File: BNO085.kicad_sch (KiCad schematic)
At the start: 0 parts

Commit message: Update schematic and libraries
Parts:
- added U5: BNO085, uSlime-libs:LGA28_5.2X3.8_CEV, symbol uSlime:BNO085
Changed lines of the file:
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@@
 	(generator_version "8.0")
 	(paper "A4")
+	(symbol
+		(lib_id "uSlime:BNO085")
+		(at 74.93 62.23 0)
+		(unit 1)
+		(exclude_from_sim no)
+		(in_bom yes)
+		(on_board yes)
+		(dnp no)
+		(fields_autoplaced yes)
+		(property "Reference" "U5"
+			(at 111.125 52.07 0)
+			(effects
+				(font
+					(size 1.524 1.524)
+				)
+			)
+		)
+		(property "Value" "BNO085"
+			(at 111.125 54.61 0)
+			(effects
+				(font
+					(size 1.524 1.524)
+				)
+			)
+		)
+		(property "Footprint" "uSlime-libs:LGA28_5.2X3.8_CEV"
+			(at 88.9 62.23 0)
+			(effects
+				(font
+					(size 1.27 1.27)
+					(italic yes)
+				)
+				(hide yes)
+			)
+		)
+		(property "Datasheet" "BNO085"
+			(at 88.9 62.23 0)
+			(effects
+				(font
+					(size 1.27 1.27)
+					(italic yes)
+				)
+				(hide yes)
+			)
+		)
+		(property "Description" ""
+			(at 88.9 62.23 0)
+			(effects
+				(font
+					(size 1.27 1.27)
+				)
+				(hide yes)
+			)
+		)
+		(pin "27"
+		)
+		(pin "24"
+		)
+		(pin "4"
+		)
+		(pin "23"
+		)
+		(pin "7"
+		)
+		(pin "28"
+		)
+		(pin "21"
+		)
+		(pin "1"
+		)
+		(pin "6"
+		)
+		(pin "10"
+		)
+		(pin "16"
+		)
+		(pin "18"
+		)
+		(pin "20"
+		)
+		(pin "11"
+		)
+		(pin "25"
+		)
+		(pin "8"
+		)
+		(pin "26"
+		)
+		(pin "13"
+		)
+		(pin "12"
+		)
+		(pin "14"
+		)
+		(pin "2"
+		)
+		(pin "3"
+		)
+		(pin "22"
+		)
+		(pin "19"
+		)
+		(pin "9"
+		)
+		(pin "15"
+		)
+		(pin "5"
+		)
+		(pin "17"
+		)
+		(instances
+			(project "uSlime"
+				(path "/f32c1c49-f803-4e7c-a530-6db148a7ba36/1072de81-ddaf-4115-9b1e-8b480e2a0117"
+					(reference "U5")
+					(unit 1)
+				)
+			)
+		)
+	)
 )

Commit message: Modify ESP32
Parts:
- added C6: 0.1 uF, Capacitor_SMD:C_0603_1608Metric, symbol uSlime:C
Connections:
- net GND: now reaches U5.10 (CLKSEL0)
- net GND: now also U5.2 (GND), U5.25 (GND)
- net +3.3V: now reaches U5.3 (VDD)
- net at U5.9 (CAP): now also C6.2

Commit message: 1st attempt finish BNO085
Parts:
- added C7, C8: 22pF, Capacitor_SMD:C_0603_1608Metric, symbol uSlime:C
- added C9: 0.1 uF, Capacitor_SMD:C_0603_1608Metric, symbol uSlime:C
- added Y1: 32.768, uSlime-libs:OSC-SMD_L3.2-W1.5, symbol uSlime:Crystal
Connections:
- net +3.3V: now also U5.28 (VDDIO), C9.1
- net GND: now also C7.1, C8.1, C9.2
- net BNO_RST: now reaches U5.11 (NRST)
- net BNO_MOSI: now reaches U5.17 (SA0/H_MOSI)
- net BNO_CS: now reaches U5.18 (H_CSN)
- net BNO_SCL: now reaches U5.19 (H_SCL/SCK/RX)
- net BNO_SDA: now reaches U5.20 (H_SDA/H_MISO/TX)
- net at U5.26 (XOUT32/CLKSEL1): now also C7.2, Y1.2
- net at U5.27 (XIN32): now also C8.2, Y1.1

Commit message: update power
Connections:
- net GND: now also C6.1
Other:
- moved on the sheet: Y1
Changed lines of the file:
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@@
 	(paper "A4")
+	(junction
+		(at 157.48 76.2)
+		(diameter 0)
+		(color 0 0 0 0)
+	)
 	(junction
 		(at 68.58 59.69)
@@
 	)
 	(junction
-		(at 157.48 77.47)
-		(diameter 0)
-		(color 0 0 0 0)
-	)
-	(junction
-		(at 165.1 77.47)
-		(diameter 0)
-		(color 0 0 0 0)
-	)
-	(junction
 		(at 83.82 64.77)
 		(diameter 0)
 		(color 0 0 0 0)
 	)
-	(wire
-		(pts
-			(xy 157.48 64.77) (xy 157.48 77.47)
+	(junction
+		(at 165.1 76.2)
+		(diameter 0)
+		(color 0 0 0 0)
+	)
+	(wire
+		(pts
+			(xy 157.48 76.2) (xy 157.48 80.01)
+		)
+		(stroke
+			(width 0)
+			(type default)
+		)
+	)
+	(wire
+		(pts
+			(xy 157.48 64.77) (xy 157.48 76.2)
 		)
 		(stroke
@@
 	(wire
 		(pts
-			(xy 165.1 77.47) (xy 165.1 80.01)
-		)
-		(stroke
-			(width 0)
-			(type default)
-		)
-	)
-	(wire
-		(pts
 			(xy 157.48 90.17) (xy 157.48 87.63)
 		)
@@
 	(wire
 		(pts
+			(xy 165.1 76.2) (xy 165.1 80.01)
+		)
+		(stroke
+			(width 0)
+			(type default)
+		)
+	)
+	(wire
+		(pts
 			(xy 80.01 64.77) (xy 83.82 64.77)
 		)
@@
 	(wire
 		(pts
+			(xy 74.93 82.55) (xy 64.77 82.55)
+		)
+		(stroke
+			(width 0)
+			(type default)
+		)
+	)
+	(wire
+		(pts
 			(xy 134.62 85.09) (xy 133.35 85.09)
 		)
@@
 	(wire
 		(pts
-			(xy 157.48 77.47) (xy 157.48 80.01)
-		)
-		(stroke
-			(width 0)
-			(type default)
-		)
-	)
-	(wire
-		(pts
 			(xy 85.09 85.09) (xy 88.9 85.09)
 		)
@@
 	(wire
 		(pts
+			(xy 64.77 82.55) (xy 64.77 87.63)
+		)
+		(stroke
+			(width 0)
+			(type default)
+		)
+	)
+	(wire
+		(pts
 			(xy 68.58 55.88) (xy 68.58 59.69)
 		)
@@
 	(wire
 		(pts
+			(xy 139.7 62.23) (xy 133.35 62.23)
+		)
+		(stroke
+			(width 0)
+			(type default)
+		)
+	)
+	(wire
+		(pts
 			(xy 134.62 87.63) (xy 133.35 87.63)
 		)
@@
 	(wire
 		(pts
+			(xy 139.7 58.42) (xy 139.7 62.23)
+		)
+		(stroke
+			(width 0)
+			(type default)
+		)
+	)
+	(wire
+		(pts
 			(xy 133.35 64.77) (xy 157.48 64.77)
 		)
@@
 	(wire
 		(pts
-			(xy 140.97 62.23) (xy 133.35 62.23)
-		)
-		(stroke
-			(width 0)
-			(type default)
-		)
-	)
-	(wire
-		(pts
-			(xy 165.1 67.31) (xy 165.1 77.47)
+			(xy 165.1 67.31) (xy 165.1 76.2)
 		)
 		(stroke
@@
 				(justify left)
 				(hide yes)
+			)
+		)
+	)
+	(symbol
+		(lib_id "power:GND")
+		(at 64.77 87.63 0)
+		(unit 1)
+		(exclude_from_sim no)
+		(in_bom yes)
+		(on_board yes)
+		(dnp no)
+		(property "Reference" "#PWR018"
+			(at 64.77 93.98 0)
+			(effects
+				(font
+					(size 1.27 1.27)
+				)
+				(hide yes)
+			)
+		)
+		(property "Value" "GND"
+			(at 63.754 84.582 90)
+			(effects
+				(font
+					(size 1.27 1.27)
+				)
+				(justify right)
+			)
+		)
+		(property "Footprint" ""
+			(at 64.77 87.63 0)
+			(effects
+				(font
+					(size 1.27 1.27)
+				)
+				(hide yes)
+			)
+		)
+		(property "Datasheet" ""
+			(at 64.77 87.63 0)
+			(effects
+				(font
+					(size 1.27 1.27)
+				)
+				(hide yes)
+			)
+		)
+		(property "Description" "Power symbol creates a global label with name \"GND\" , ground"
+			(at 64.77 87.63 0)
+			(effects
+				(font
+					(size 1.27 1.27)
+				)
+				(hide yes)
+			)
+		)
+		(pin "1"
+		)
+		(instances
+			(project "uSlime"
+				(path "/f32c1c49-f803-4e7c-a530-6db148a7ba36/1072de81-ddaf-4115-9b1e-8b480e2a0117"
+					(reference "#PWR018")
+					(unit 1)
+				)
 			)
 		)
@@
 	(symbol
 		(lib_id "uSlime:Crystal")
-		(at 161.29 77.47 0)
+		(at 161.29 76.2 0)
 		(unit 1)
 		(exclude_from_sim no)
@@
 		(fields_autoplaced yes)
 		(property "Reference" "Y1"
-			(at 161.29 69.85 0)
+			(at 161.29 68.58 0)
 			(effects
 				(font
@@
 		)
 		(property "Value" "32.768"
-			(at 161.29 72.39 0)
+			(at 161.29 71.12 0)
 			(effects
 				(font
@@
 		)
 		(property "Footprint" "uSlime-libs:OSC-SMD_L3.2-W1.5"
-			(at 161.29 77.47 0)
+			(at 161.29 76.2 0)
 			(effects
 				(font
@@
 		)
 		(property "Datasheet" "~"
-			(at 161.29 77.47 0)
+			(at 161.29 76.2 0)
 			(effects
 				(font
@@
 		)
 		(property "Description" "Two pin crystal"
-			(at 161.29 77.47 0)
+			(at 161.29 76.2 0)
 			(effects
 				(font
@@
 	(symbol
 		(lib_id "power:+3.3V")
-		(at 140.97 62.23 0)
+		(at 139.7 58.42 0)
 		(unit 1)
 		(exclude_from_sim no)
@@
 		(dnp no)
 		(property "Reference" "#PWR014"
-			(at 140.97 66.04 0)
+			(at 139.7 62.23 0)
 			(effects
 				(font
@@
 		)
 		(property "Value" "+3.3V"
-			(at 133.858 60.96 0)
+			(at 132.588 57.15 0)
 			(effects
 				(font
@@
 		)
 		(property "Footprint" ""
-			(at 140.97 62.23 0)
+			(at 139.7 58.42 0)
 			(effects
 				(font
@@
 		)
 		(property "Datasheet" ""
-			(at 140.97 62.23 0)
+			(at 139.7 58.42 0)
 			(effects
 				(font
@@
 		)
 		(property "Description" "Power symbol creates a global label with name \"+3.3V\""
-			(at 140.97 62.23 0)
-			(effects
-				(font
+			(at 139.7 58.42 0)
+			(effects
+				(font

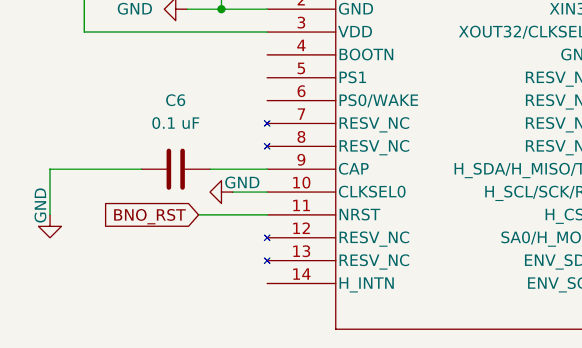
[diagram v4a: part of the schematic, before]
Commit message: Condense schematic
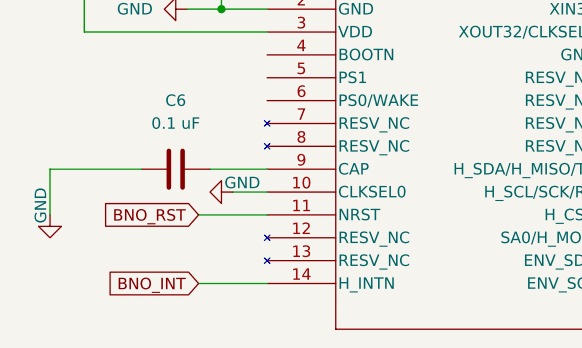
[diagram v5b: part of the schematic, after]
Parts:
- C6, C7, C8, C9: footprint Capacitor_SMD:C_0603_1608Metric -> Capacitor_SMD:C_0402_1005Metric
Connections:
- net BNO_INT: now reaches U5.14 (H_INTN)
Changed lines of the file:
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@@
+	(wire
+		(pts
+			(xy 81.28 95.25) (xy 88.9 95.25)
+		)
+		(stroke
+			(width 0)
+			(type default)
+		)
+	)
 	(wire
 		(pts
@@
 		(property "Intersheetrefs" "${INTERSHEET_REFS}"
 			(at 69.9491 87.63 0)
+			(effects
+				(font
+					(size 1.27 1.27)
+				)
+				(justify right)
+				(hide yes)
+			)
+		)
+	)
+	(global_label "BNO_INT"
+		(shape input)
+		(at 81.28 95.25 180)
+		(fields_autoplaced yes)
+		(effects
+			(font
+				(size 1.27 1.27)
+			)
+			(justify right)
+		)
+		(property "Intersheetrefs" "${INTERSHEET_REFS}"
+			(at 70.4933 95.25 0)
 			(effects
 				(font
@@
 			)
 		)
-		(property "Footprint" "Capacitor_SMD:C_0603_1608Metric"
+		(property "Footprint" "Capacitor_SMD:C_0402_1005Metric"
 			(at 82.55 81.5848 0)
 			(effects
@@
 			)
 		)
-		(property "Footprint" "Capacitor_SMD:C_0603_1608Metric"
+		(property "Footprint" "Capacitor_SMD:C_0402_1005Metric"
 			(at 164.1348 80.01 0)
 			(effects
@@
 			)
 		)
-		(property "Footprint" "Capacitor_SMD:C_0603_1608Metric"
+		(property "Footprint" "Capacitor_SMD:C_0402_1005Metric"
 			(at 156.5148 80.01 0)
 			(effects
@@
 			)
 		)
-		(property "Footprint" "Capacitor_SMD:C_0603_1608Metric"
+		(property "Footprint" "Capacitor_SMD:C_0402_1005Metric"
 			(at 80.01 58.7248 0)
 			(effects

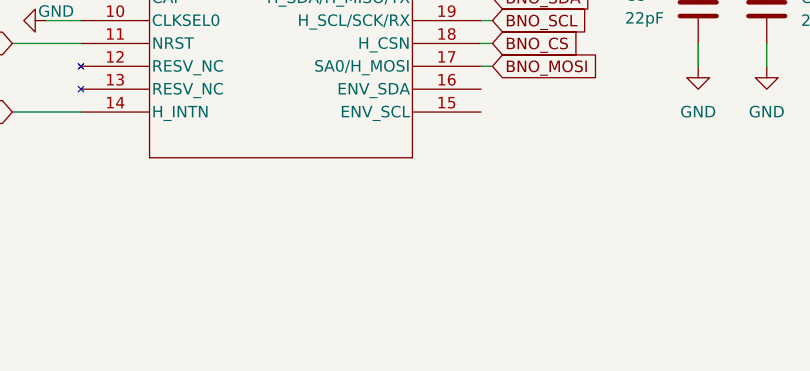
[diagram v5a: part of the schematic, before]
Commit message: Add connector for testing
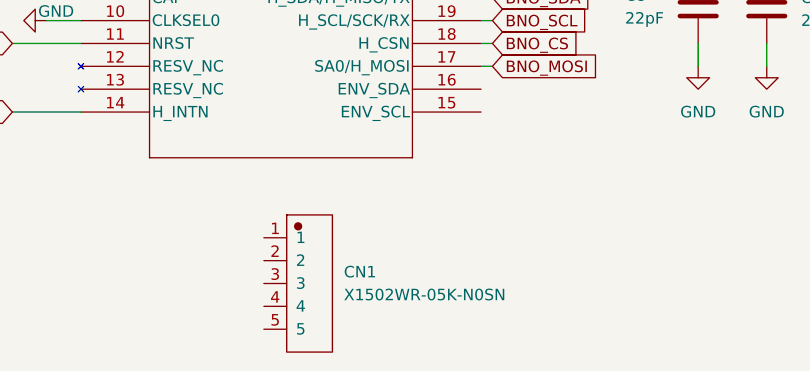
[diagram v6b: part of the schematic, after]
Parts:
- added CN1: X1502WR-05K-N0SN, uSlime-libs:CONN-TH_5P-P1.50_X1502WR-05K-N0SN, symbol uSlime:X1502WR-05K-N0SN
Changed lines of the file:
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@@
+	)
+	(symbol
+		(lib_id "uSlime:X1502WR-05K-N0SN")
+		(at 114.3 114.3 0)
+		(unit 1)
+		(exclude_from_sim no)
+		(in_bom yes)
+		(on_board yes)
+		(dnp no)
+		(fields_autoplaced yes)
+		(property "Reference" "CN1"
+			(at 118.11 113.0299 0)
+			(effects
+				(font
+					(size 1.27 1.27)
+				)
+				(justify left)
+			)
+		)
+		(property "Value" "X1502WR-05K-N0SN"
+			(at 118.11 115.5699 0)
+			(effects
+				(font
+					(size 1.27 1.27)
+				)
+				(justify left)
+			)
+		)
+		(property "Footprint" "uSlime-libs:CONN-TH_5P-P1.50_X1502WR-05K-N0SN"
+			(at 114.3 109.22 0)
+			(effects
+				(font
+					(size 1.27 1.27)
+				)
+				(hide yes)
+			)
+		)
+		(property "Datasheet" "http://www.szlcsc.com/product/details_587019.html"
+			(at 114.3 114.3 0)
+			(effects
+				(font
+					(size 1.27 1.27)
+				)
+				(hide yes)
+			)
+		)
+		(property "Description" "C561537"
+			(at 114.3 119.38 0)
+			(effects
+				(font
+					(size 1.27 1.27)
+				)
+				(hide yes)
+			)
+		)
+		(property "uuid" "std:268fd150cfff42dfa6c6c0b3cfd730b2"
+			(at 114.3 119.38 0)
+			(effects
+				(font
+					(size 1.27 1.27)
+				)
+				(hide yes)
+			)
+		)
+		(pin "3"
+		)
+		(pin "4"
+		)
+		(pin "2"
+		)
+		(pin "1"
+		)
+		(pin "5"
+		)
+		(instances
+			(project "uSlime"
+				(path "/f32c1c49-f803-4e7c-a530-6db148a7ba36/1072de81-ddaf-4115-9b1e-8b480e2a0117"
+					(reference "CN1")
+					(unit 1)
+				)
+			)
+		)
 	)
 	(symbol

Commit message: Create prelim PCB
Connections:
- net +3.3V: now also CN1.2
- net BNO_SCL: now also CN1.5
- net BNO_SDA: now also CN1.1
- net GND: now also CN1.4
- net BNO_INT2: now reaches CN1.3
- net BNO_CS: no longer names the net of U5.18 (H_CSN)
- net BNO_MOSI: no longer names the net of U5.17 (SA0/H_MOSI)
- net BNO_RST: no longer names the net of U5.11 (NRST)
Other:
- moved on the sheet: C6, C7, C8, C9, CN1, U5, Y1
